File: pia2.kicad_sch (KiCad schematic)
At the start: 41 parts, among them IC25 LM393P, IC31 74LS02N, IC34 MC14050BCP, IC35 MC6821

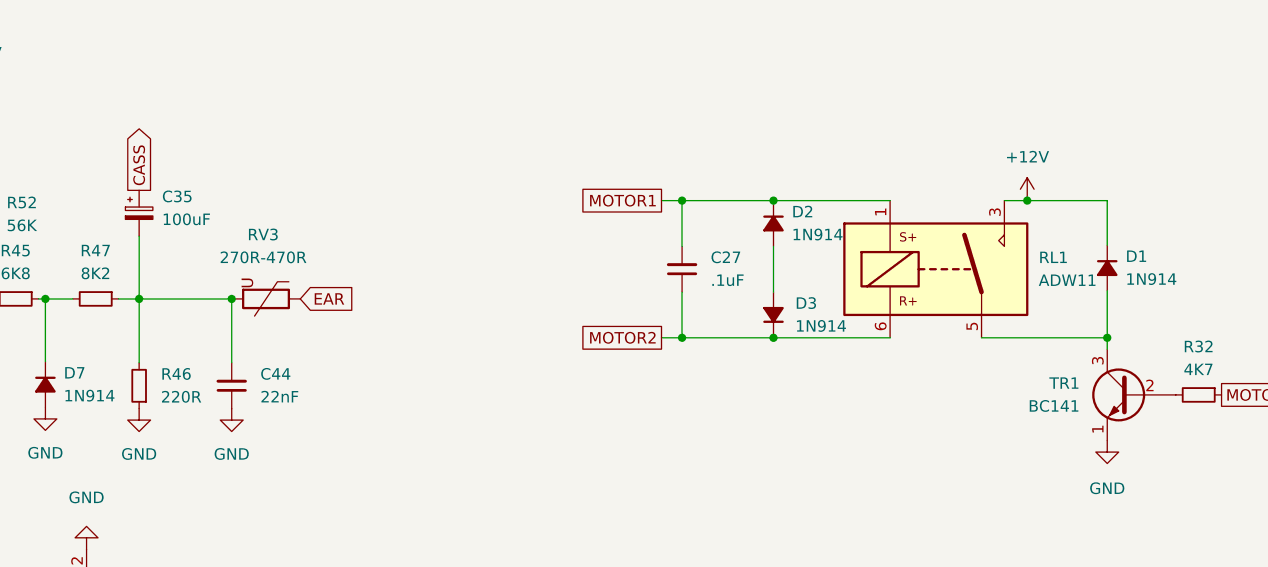
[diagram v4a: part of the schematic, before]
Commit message: update part numbers
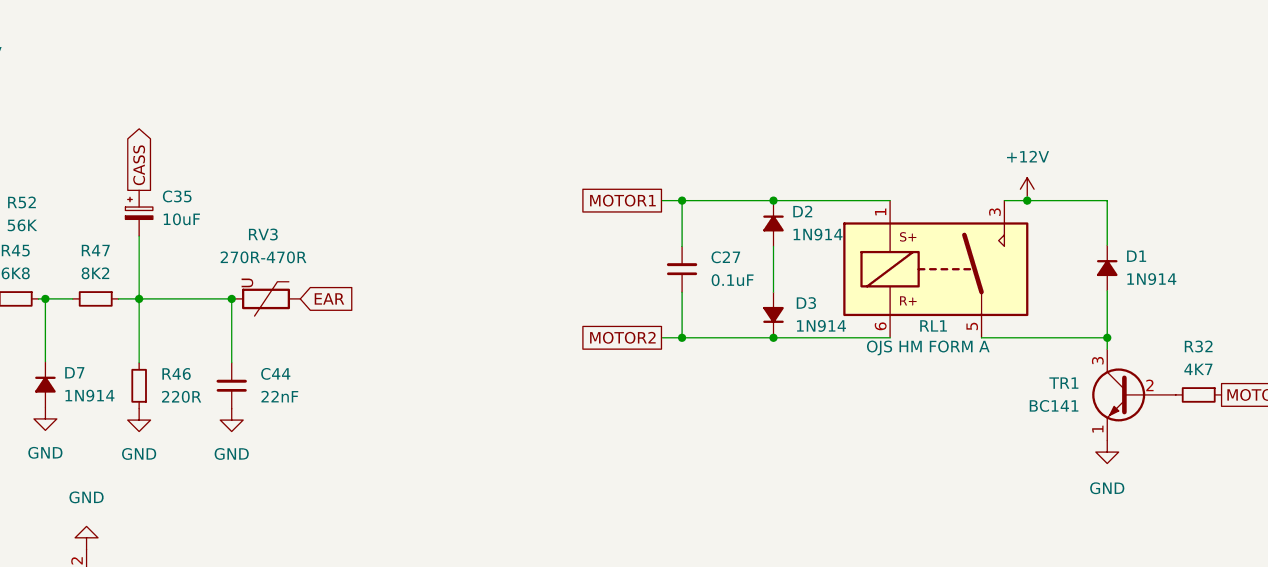
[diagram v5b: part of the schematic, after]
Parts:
- C27: value .1uF -> 0.1uF; DigiKey (none) -> BC1101CT-ND
- C35: value 100uF -> 10uF; DigiKey 732-8598-1-ND -> 732-8593-1-ND
- C48: DigiKey (none) -> 399-13930-1-ND
- D1, D2, D3, D7: DigiKey (none) -> 1N914FS-ND
- IC25: DigiKey (none) -> 296-1398-5-ND
- IC31: DigiKey (none) -> 296-1627-5-ND
- IC34: DigiKey (none) -> 296-2056-ND; Note (none) -> obsolete use CD4050B or convert MC14050BDG
- RL1: value ADW11 -> OJS HM FORM A; footprint Relay_THT:Relay_1P1T_NO_10x24x18.8mm_Panasonic_ADW11xxxxW_THT -> Dragon:OJS HM 10A Relay
- TR1: DigiKey (none) -> KSD1616AYTACT-ND; Note (none) -> use KSD1616AYTA instead
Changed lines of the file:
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@@
       (effects (font (size 1.27 1.27)) (justify right))
     )
-    (property "Value" ".1uF" (id 1) (at 193.04 134.6135 0)
+    (property "Value" "0.1uF" (id 1) (at 193.04 134.6135 0)
       (effects (font (size 1.27 1.27)) (justify right))
     )
@@
       (effects (font (size 1.27 1.27)) hide)
     )
-    (property "Datasheet" "~" (id 3) (at 189.865 133.35 0)
+    (property "Datasheet" "https://www.vishay.com/docs/45171/kseries.pdf" (id 3) (at 189.865 133.35 0)
+      (effects (font (size 1.27 1.27)) hide)
+    )
+    (property "DigiKey" "BC1101CT-ND" (id 4) (at 189.865 133.35 0)
       (effects (font (size 1.27 1.27)) hide)
     )
@@
       (effects (font (size 1.27 1.27)) hide)
     )
-    (property "Datasheet" "~" (id 3) (at 119.126 146.177 90)
+    (property "Datasheet" "http://www.vishay.com/docs/85622/1n914.pdf" (id 3) (at 119.126 146.177 90)
+      (effects (font (size 1.27 1.27)) hide)
+    )
+    (property "DigiKey" "1N914FS-ND" (id 4) (at 119.126 146.177 0)
       (effects (font (size 1.27 1.27)) hide)
     )
@@
       (effects (font (size 1.27 1.27)) (justify left) hide)
     )
+    (property "DigiKey" "KSD1616AYTACT-ND" (id 4) (at 239.649 147.32 0)
+      (effects (font (size 1.27 1.27)) hide)
+    )
+    (property "Note" "use KSD1616AYTA instead" (id 5) (at 239.649 147.32 0)
+      (effects (font (size 1.27 1.27)) hide)
+    )
     (pin "1")
     (pin "2")
@@
   )
   (symbol (lib_id "Relay:ADW11") (at 218.059 133.35 0) (unit 1)
-    (in_bom yes) (on_board yes) (fields_autoplaced)
-    (property "Reference" "RL1" (id 0) (at 229.489 132.0799 0)
-      (effects (font (size 1.27 1.27)) (justify left))
-    )
-    (property "Value" "ADW11" (id 1) (at 229.489 134.6199 0)
-      (effects (font (size 1.27 1.27)) (justify left))
-    )
-    (property "Footprint" "Relay_THT:Relay_1P1T_NO_10x24x18.8mm_Panasonic_ADW11xxxxW_THT" (id 2) (at 251.714 134.62 0)
-      (effects (font (size 1.27 1.27)) hide)
-    )
-    (property "Datasheet" "https://www.panasonic-electric-works.com/pew/es/downloads/ds_dw_hl_en.pdf" (id 3) (at 218.059 133.35 0)
+    (in_bom yes) (on_board yes)
+    (property "Reference" "RL1" (id 0) (at 216.154 139.7 0)
+      (effects (font (size 1.27 1.27)) (justify left))
+    )
+    (property "Value" "OJS HM FORM A" (id 1) (at 210.312 141.986 0)
+      (effects (font (size 1.27 1.27)) (justify left))
+    )
+    (property "Footprint" "Dragon:OJS HM 10A Relay" (id 2) (at 251.714 134.62 0)
+      (effects (font (size 1.27 1.27)) hide)
+    )
+    (property "Datasheet" "https://www.te.com/commerce/DocumentDelivery/DDEController?Action=srchrtrv&DocNm=OJS_10A&DocType=DS&DocLang=English" (id 3) (at 218.059 133.35 0)
       (effects (font (size 1.27 1.27)) hide)
     )
@@
       (effects (font (size 1.27 1.27)) hide)
     )
-    (property "Datasheet" "~" (id 3) (at 237.109 133.223 90)
+    (property "Datasheet" "http://www.vishay.com/docs/85622/1n914.pdf" (id 3) (at 237.109 133.223 90)
+      (effects (font (size 1.27 1.27)) hide)
+    )
+    (property "DigiKey" "1N914FS-ND" (id 4) (at 237.109 133.223 0)
       (effects (font (size 1.27 1.27)) hide)
     )
@@
       (effects (font (size 1.27 1.27)) hide)
     )
-    (property "Datasheet" "~" (id 3) (at 33.401 139.319 0)
+    (property "Datasheet" "https://connect.kemet.com:7667/gateway/IntelliData-ComponentDocumentation/1.0/download/datasheet/C315C220K2G5TA7301" (id 3) (at 33.401 139.319 0)
+      (effects (font (size 1.27 1.27)) hide)
+    )
+    (property "DigiKey" "399-13930-1-ND" (id 4) (at 33.401 139.319 0)
       (effects (font (size 1.27 1.27)) hide)
     )
@@
       (effects (font (size 1.27 1.27)) hide)
     )
-    (property "Datasheet" "~" (id 3) (at 200.025 128.27 90)
+    (property "Datasheet" "http://www.vishay.com/docs/85622/1n914.pdf" (id 3) (at 200.025 128.27 90)
+      (effects (font (size 1.27 1.27)) hide)
+    )
+    (property "DigiKey" "1N914FS-ND" (id 4) (at 200.025 128.27 0)
       (effects (font (size 1.27 1.27)) hide)
     )
@@
     )
     (property "Datasheet" "https://media.digikey.com/pdf/Data%20Sheets/ON%20Semiconductor%20PDFs/MC14049B,50B_Rev7.pdf" (id 3) (at 234.696 53.34 0)
+      (effects (font (size 1.27 1.27)) hide)
+    )
+    (property "DigiKey" "296-2056-ND" (id 4) (at 234.696 44.45 0)
+      (effects (font (size 1.27 1.27)) hide)
+    )
+    (property "Note" "obsolete use CD4050B or convert MC14050BDG" (id 5) (at 234.696 44.45 0)
       (effects (font (size 1.27 1.27)) hide)
     )
@@
       (effects (font (size 1.27 1.27)) hide)
     )
-    (property "Datasheet" "~" (id 3) (at 200.025 138.43 90)
+    (property "Datasheet" "http://www.vishay.com/docs/85622/1n914.pdf" (id 3) (at 200.025 138.43 90)
+      (effects (font (size 1.27 1.27)) hide)
+    )
+    (property "DigiKey" "1N914FS-ND" (id 4) (at 200.025 138.43 0)
       (effects (font (size 1.27 1.27)) hide)
     )
@@
     )
     (property "Datasheet" "http://www.ti.com/lit/gpn/sn74ls02" (id 3) (at 115.824 46.482 0)
+      (effects (font (size 1.27 1.27)) hide)
+    )
+    (property "DigiKey" "296-1627-5-ND" (id 4) (at 115.824 46.482 0)
       (effects (font (size 1.27 1.27)) hide)
     )
@@
       (effects (font (size 1.27 1.27)) hide)
     )
+    (property "DigiKey" "296-1398-5-ND" (id 4) (at 96.52 134.112 0)
+      (effects (font (size 1.27 1.27)) hide)
+    )
     (pin "1")
     (pin "2")
@@
       (effects (font (size 1.27 1.27)) (justify left))
     )
-    (property "Value" "100uF" (id 1) (at 132.08 127.8508 0)
+    (property "Value" "10uF" (id 1) (at 132.08 127.8508 0)
       (effects (font (size 1.27 1.27)) (justify left))
     )
@@
       (effects (font (size 1.27 1.27)) hide)
     )
-    (property "Datasheet" "https://www.we-online.com/katalog/datasheet/860010372006.pdf" (id 3) (at 129.54 127.127 0)
-      (effects (font (size 1.27 1.27)) hide)
-    )
-    (property "DigiKey" "732-8598-1-ND" (id 4) (at 129.54 127.127 0)
-      (effects (font (size 1.27 1.27)) hide)
-    )
+    (property "Datasheet" "https://www.we-online.com/katalog/datasheet/860010372001.pdf" (id 3) (at 129.54 127.127 0)
+      (effects (font (size 1.27 1.27)) hide)
+    )
+    (property "DigiKey" "732-8593-1-ND" (id 4) (at 129.54 127.127 0)
+      (effects (font (size 1.27 1.27)) hide)
+    )

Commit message: resolve part numbers
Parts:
- IC35: DigiKey (none) -> 2156-MC6821CS-2156-ND; Note (none) -> donor is preferable
- PL4: Note (none) -> RS Components
- R16: DigiKey (none) -> CF14JT33K0CT-ND
- R29: DigiKey (none) -> CF14JT68K0CT-ND
- R32, R38, R63: DigiKey (none) -> CF14JT4K70CT-ND
- R45: DigiKey (none) -> CF14JT6K80CT-ND
- R46: DigiKey (none) -> CF14JT220RCT-ND
- R47: DigiKey (none) -> CF14JT8K20CT-ND
- R48: DigiKey (none) -> CF14JT15K0CT-ND
- R49: DigiKey (none) -> CF14JT1K00CT-ND
- R50, R52: DigiKey (none) -> CF14JT56K0CT-ND
- R51: DigiKey (none) -> CF14JT1M50CT-ND
- R56: DigiKey (none) -> CF14JT10K0CT-ND
- R57: DigiKey (none) -> RNF14FTD20K0CT-ND
- R58: DigiKey (none) -> RNF14FTD80K6CT-ND
- R59: DigiKey (none) -> S160CACT-ND
- R60: DigiKey (none) -> S330KCACT-ND
- R61: DigiKey (none) -> RNF14FTD41K2CT-ND; Note (none) -> 40K2 not availalbe from digikey in 1% tolerance
- R62: DigiKey (none) -> RNF14FTD10K0CT-ND
- R64: DigiKey (none) -> CF14JT100KCT-ND
- RL1: DigiKey (none) -> 41-OJS-SH-105HMF,00000-ND
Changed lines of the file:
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@@
+      (effects (font (size 1.27 1.27)) hide)
+    )
+    (property "DigiKey" "S160CACT-ND" (id 4) (at 253.619 39.37 0)
       (effects (font (size 1.27 1.27)) hide)
     )
@@
       (effects (font (size 1.27 1.27)) hide)
     )
+    (property "DigiKey" "S330KCACT-ND" (id 4) (at 253.619 52.07 0)
+      (effects (font (size 1.27 1.27)) hide)
+    )
     (pin "1")
     (pin "2")
@@
       (effects (font (size 1.27 1.27)) hide)
     )
+    (property "DigiKey" "RNF14FTD10K0CT-ND" (id 4) (at 253.619 46.99 0)
+      (effects (font (size 1.27 1.27)) hide)
+    )
     (pin "1")
     (pin "2")
@@
     )
     (property "Datasheet" "~" (id 3) (at 247.269 147.32 0)
+      (effects (font (size 1.27 1.27)) hide)
+    )
+    (property "DigiKey" "CF14JT4K70CT-ND" (id 4) (at 247.269 147.32 0)
       (effects (font (size 1.27 1.27)) hide)
     )
@@
       (effects (font (size 1.27 1.27)) hide)
     )
+    (property "DigiKey" "RNF14FTD80K6CT-ND" (id 4) (at 253.619 41.91 0)
+      (effects (font (size 1.27 1.27)) hide)
+    )
     (pin "1")
     (pin "2")
@@
       (effects (font (size 1.27 1.27)) hide)
     )
+    (property "DigiKey" "41-OJS-SH-105HMF,00000-ND" (id 4) (at 218.059 133.35 0)
+      (effects (font (size 1.27 1.27)) hide)
+    )
     (pin "1")
     (pin "3")
@@
       (effects (font (size 1.27 1.27)) hide)
     )
+    (property "DigiKey" "CF14JT1M50CT-ND" (id 4) (at 96.012 121.793 0)
+      (effects (font (size 1.27 1.27)) hide)
+    )
     (pin "1")
     (pin "2")
@@
       (effects (font (size 1.27 1.27)) hide)
     )
+    (property "Note" "RS Components" (id 4) (at 123.698 172.085 0)
+      (effects (font (size 1.27 1.27)) hide)
+    )
     (pin "1")
     (pin "2")
@@
       (effects (font (size 1.27 1.27)) hide)
     )
+    (property "DigiKey" "CF14JT220RCT-ND" (id 4) (at 129.54 146.304 0)
+      (effects (font (size 1.27 1.27)) hide)
+    )
     (pin "1")
     (pin "2")
@@
       (effects (font (size 1.27 1.27)) hide)
     )
+    (property "DigiKey" "CF14JT6K80CT-ND" (id 4) (at 115.824 136.652 0)
+      (effects (font (size 1.27 1.27)) hide)
+    )
     (pin "1")
     (pin "2")
@@
     )
     (property "Datasheet" "~" (id 3) (at 105.156 117.856 0)
+      (effects (font (size 1.27 1.27)) hide)
+    )
+    (property "DigiKey" "CF14JT56K0CT-ND" (id 4) (at 105.156 117.856 0)
       (effects (font (size 1.27 1.27)) hide)
     )
@@
       (effects (font (size 1.27 1.27)) hide)
     )
+    (property "DigiKey" "RNF14FTD41K2CT-ND" (id 4) (at 253.619 49.53 0)
+      (effects (font (size 1.27 1.27)) hide)
+    )
+    (property "Note" "40K2 not availalbe from digikey in 1% tolerance" (id 5) (at 253.619 49.53 0)
+      (effects (font (size 1.27 1.27)) hide)
+    )
     (pin "1")
     (pin "2")
@@
     )
     (property "Datasheet" "~" (id 3) (at 112.395 127.254 0)
+      (effects (font (size 1.27 1.27)) hide)
+    )
+    (property "DigiKey" "CF14JT56K0CT-ND" (id 4) (at 112.395 127.254 0)
       (effects (font (size 1.27 1.27)) hide)
     )
@@
       (effects (font (size 1.27 1.27)) hide)
     )
+    (property "DigiKey" "CF14JT100KCT-ND" (id 4) (at 264.16 34.29 0)
+      (effects (font (size 1.27 1.27)) hide)
+    )
     (pin "1")
     (pin "2")
@@
     )
     (property "Datasheet" "~" (id 3) (at 29.972 78.232 0)
+      (effects (font (size 1.27 1.27)) hide)
+    )
+    (property "DigiKey" "CF14JT4K70CT-ND" (id 4) (at 29.972 78.232 0)
       (effects (font (size 1.27 1.27)) hide)
     )
@@
     )
     (property "Datasheet" "~" (id 3) (at 253.619 44.45 0)
+      (effects (font (size 1.27 1.27)) hide)
+    )
+    (property "DigiKey" "RNF14FTD20K0CT-ND" (id 4) (at 253.619 44.45 0)
       (effects (font (size 1.27 1.27)) hide)
     )
@@
       (effects (font (size 1.27 1.27)) hide)
     )
+    (property "DigiKey" "CF14JT10K0CT-ND" (id 4) (at 86.233 74.422 0)
+      (effects (font (size 1.27 1.27)) hide)
+    )
     (pin "1")
     (pin "2")
@@
       (effects (font (size 1.27 1.27)) hide)
     )
+    (property "DigiKey" "CF14JT8K20CT-ND" (id 4) (at 124.714 136.652 0)
+      (effects (font (size 1.27 1.27)) hide)
+    )
     (pin "1")
     (pin "2")
@@
       (effects (font (size 1.27 1.27)) hide)
     )
+    (pin "1")
+    (pin "2")
+    (pin "3")
+    (pin "4")
+    (pin "5")
+    (pin "6")
     (pin "10")
     (pin "8")
     (pin "9")
+    (pin "11")
+    (pin "12")
+    (pin "13")
+    (pin "14")
+    (pin "7")
   )
   (symbol (lib_id "Jumper:Jumper_3_Bridged12") (at 91.44 40.132 270) (mirror x) (unit 1)
@@
     )
     (property "Datasheet" "" (id 3) (at 59.69 64.262 0)
+      (effects (font (size 1.27 1.27)) hide)
+    )
+    (property "DigiKey" "2156-MC6821CS-2156-ND" (id 4) (at 59.69 64.262 0)
+      (effects (font (size 1.27 1.27)) hide)
+    )
+    (property "Note" "donor is preferable" (id 5) (at 59.69 64.262 0)
       (effects (font (size 1.27 1.27)) hide)
     )
@@
     (pin "2")
     (pin "3")
+    (pin "5")
+    (pin "6")
+    (pin "7")
+    (pin "4")
+    (pin "8")
   )
   (symbol (lib_id "Device:R_Small") (at 36.449 132.969 270) (unit 1)
@@
       (effects (font (size 1.27 1.27)) hide)
     )
+    (property "DigiKey" "CF14JT68K0CT-ND" (id 4) (at 36.449 132.969 0)
+      (effects (font (size 1.27 1.27)) hide)
+    )
     (pin "1")
     (pin "2")
@@
     )
     (property "Datasheet" "~" (id 3) (at 54.356 139.319 0)
+      (effects (font (size 1.27 1.27)) hide)
+    )
+    (property "DigiKey" "CF14JT33K0CT-ND" (id 4) (at 54.356 139.319 0)
       (effects (font (size 1.27 1.27)) hide)
     )
@@
       (effects (font (size 1.27 1.27)) hide)
     )
+    (property "DigiKey" "CF14JT4K70CT-ND" (id 4) (at 127.762 46.482 0)
+      (effects (font (size 1.27 1.27)) hide)
+    )
     (pin "1")
     (pin "2")
@@
       (effects (font (size 1.27 1.27)) hide)
     )
+    (property "DigiKey" "CF14JT1K00CT-ND" (id 4) (at 87.757 117.983 0)
+      (effects (font (size 1.27 1.27)) hide)
+    )
     (pin "1")
     (pin "2")
@@
       (effects (font (size 1.27 1.27)) hide)
     )
+    (property "DigiKey" "CF14JT15K0CT-ND" (id 4) (at 105.156 146.05 0)
+      (effects (font (size 1.27 1.27)) hide)
+    )
